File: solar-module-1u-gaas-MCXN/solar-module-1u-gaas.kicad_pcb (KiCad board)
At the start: 4 copper layers, 83 x 100 mm, 110 parts, among them J1 MMS-104-01-[F/L]-SH, J2 M55-6021242R, J4 SM14B-SHLS-TF, Q1 NTR4101P, Q2 DMP2240UDM-7, U1 MCXN947VKLT, U10 TPS63060DSCR, U11 TCAN330, U12 LTC4412, U2 TMP101NA/3KSLOTTED, U3 LT1618EMSTRPBF, U4 INA226, U7 TMP101NA/3KSLOTTED, Y2 24 MHz

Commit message: Now solar module v1.2.
Upgraded CAN transciever to the 337, added version bits, removed silkscreen on cell outlines, double checked fastener heads, cleaned up documentation a lot, fixed ERCs and DRCs.
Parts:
- C13, C20, C4: footprint oresat-passives:0603-C-NOSILK -> oresat-passives:0805-C-NOSILK
- C15, C19, C23, C29: footprint oresat-passives:0805-C-NOSILK -> oresat-passives:1206-C
- D4, D7: value AMBER -> AMB
- U11: value TCAN330 -> TCAN337G
- U4: footprint Package_SO:VSSOP-10_3x3mm_P0.5mm -> Package_SO:TSSOP-10_3x3mm_P0.5mm
- moved C28 68.8 mm to (168.9, 135.9), turned to -90 degrees
- moved U11 65.3 mm to (168.5, 132.3), turned to 90 degrees
- moved R20 2.20 mm to (122.4, 65.9)
- moved C23 2.07 mm to (122.7, 64.0)
- moved C26 1.47 mm to (136.7, 138.5)
- moved C3 1.20 mm to (145.8, 91.8)
- moved C29 1.15 mm to (135.1, 139.2)
- moved C50 0.90 mm to (138.6, 139.4), turned to -90 degrees
- moved L3 0.63 mm to (135.1, 135.4)
- moved C13 0.36 mm to (119.3, 67.9)
- moved C4 0.32 mm to (137.4, 75.3)
- moved C49 0.23 mm to (138.1, 141.5)
- moved C53 0.23 mm to (138.1, 145.0)
- moved C19 0.11 mm to (118.7, 64.1)
- moved C15 0.10 mm to (118.7, 66.1)
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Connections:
- net Net-(U1C-P1_13) renamed /Microcontroller/MCU-LED
- U1 pad 5: unconnected-(U1C-P1_12-Pad5) -> /Microcontroller/CAN-FAULT
- U1 pad 7: unconnected-(U1C-P1_14-Pad7) -> /Microcontroller/CAN-SILENT
- U1 pad 89: unconnected-(U1B-P0_21-Pad89) -> GND
- U1 pad 90: unconnected-(U1B-P0_22-Pad90) -> GND
- U1 pad 91: unconnected-(U1B-P0_23-Pad91) -> GND
- U11 pad 5: unconnected-(U11-SHDN-Pad5) -> /Microcontroller/CAN-FAULT
- U11 pad 8: unconnected-(U11-S-Pad8) -> /Microcontroller/CAN-SILENT
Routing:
- net Net-(U11-TXD): track 94.8 -> 21.3 mm
- net /CAN_L: track 12.6 -> 85.7 mm
- net /CAN_H: track 14.1 -> 86.4 mm
- net Net-(U11-RXD): track 96.9 -> 25.0 mm
- net /Microcontroller/CAN-FAULT: track 0.00 -> 29.2 mm, vias 0 -> 2
- net /Microcontroller/CAN-SILENT: track 0.00 -> 24.9 mm, vias 0 -> 2
- net GND: track 14.2 -> 4.72 mm, vias 1362 -> 1365
- net +3.3V: track 58.7 -> 50.4 mm, vias 38 -> 37
- net /MPPT and Power/TPS-VOUT-3.3V: track 9.23 -> 11.5 mm
- net VDD_CORE: track 25.0 -> 23.6 mm
- net Net-(U10-VIN): track 1.85 -> 0.49 mm

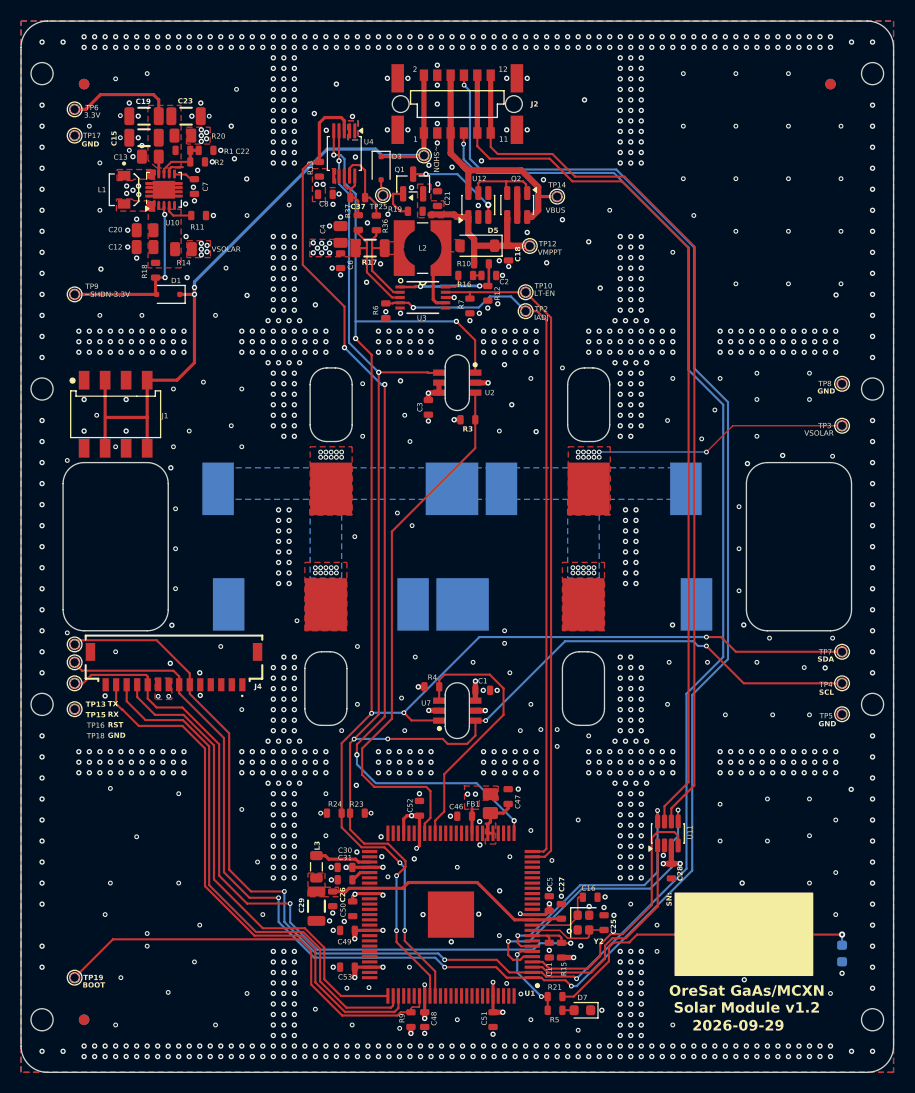
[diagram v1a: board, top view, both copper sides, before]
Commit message: Updated fastener keepouts from Sam
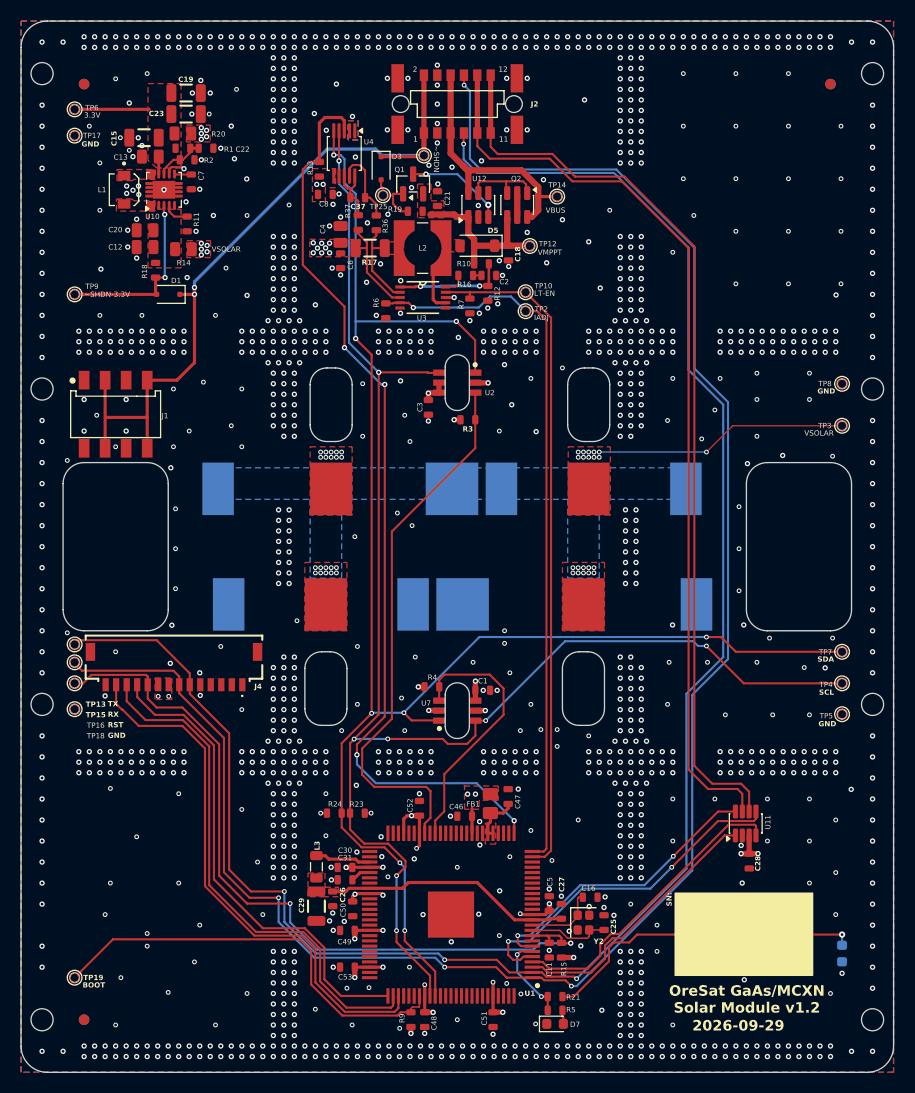
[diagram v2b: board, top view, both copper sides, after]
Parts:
- moved C28 7.46 mm to (176.3, 134.9)
- moved U11 7.46 mm to (175.9, 131.3)
- moved C19 4.57 mm to (122.7, 61.9), turned to 0 degrees
- moved D7 2.91 mm to (157.8, 150.4), turned to 0 degrees
- moved R11 1.36 mm to (122.8, 74.3), turned to 90 degrees
- moved R2 1.02 mm to (122.8, 68.2)
- moved C7 0.53 mm to (123.2, 70.3)
- moved C22 0.20 mm to (124.6, 67.1)
- moved R1 0.20 mm to (122.4, 67.1)
- moved R20 0.20 mm to (122.4, 65.7)
- moved C23 0.20 mm to (122.7, 63.9)
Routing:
- net Net-(U11-TXD): track 21.3 -> 25.7 mm
- net Net-(U11-RXD): track 25.0 -> 28.8 mm
- net /Microcontroller/CAN-FAULT: track 29.2 -> 33.0 mm
- net /MPPT and Power/TPS-VOUT-3.3V: track 11.5 -> 8.24 mm
- net /Microcontroller/CAN-SILENT: track 24.9 -> 27.8 mm
- net /CAN_L: track 85.7 -> 87.7 mm
- net /CAN_H: track 86.4 -> 88.2 mm
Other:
- board text added: "Group on User.Drawings is the amalgamation of all wedge fasteners that a solar module should encounter on a 1, 2, and 3U structure. Keep components out of that as much as possible. C7 and J4 currently are the only visible issues, and should be OK."
